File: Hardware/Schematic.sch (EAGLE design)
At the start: 15 parts, among them J1 691311400102, J2 691311400102, K1 ZF112, T1 BC547, U1 HLK-PM01, U2 ESP32-DEVKIT-V1

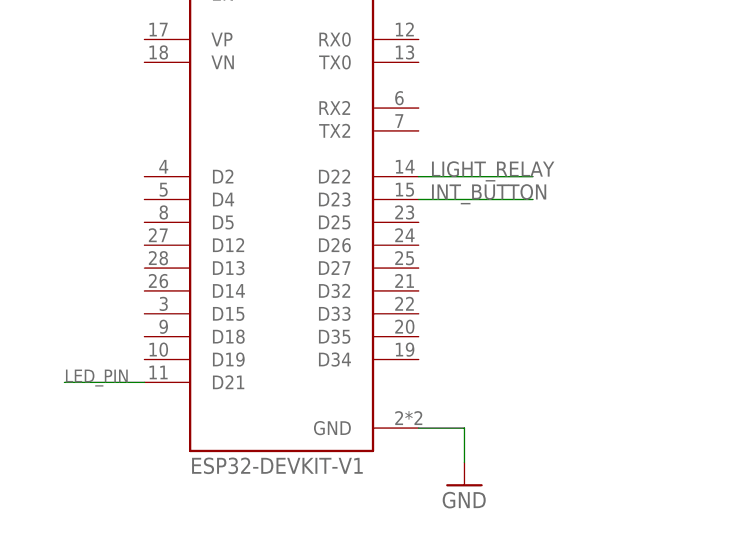
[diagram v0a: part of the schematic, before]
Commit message: Add Interrupt to wake from deep sleep to change the configuration settings
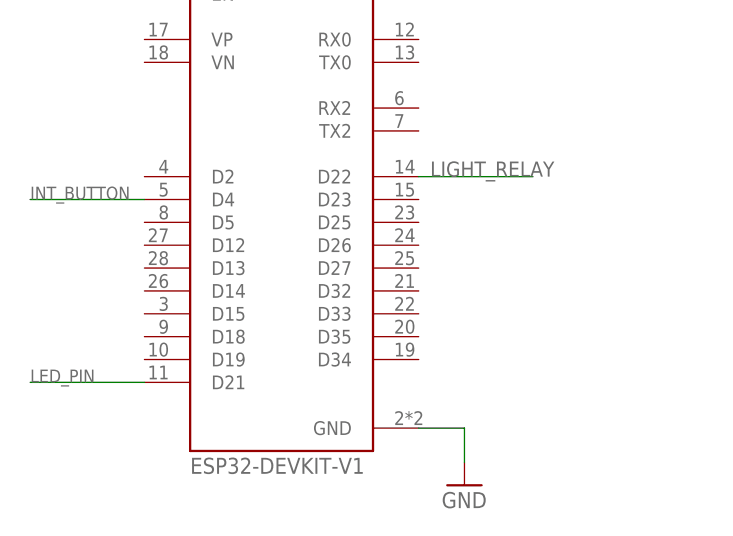
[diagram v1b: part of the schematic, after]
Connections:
- net INT_BUTTON: now also U2.D4; no longer U2.D23
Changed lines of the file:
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@@
 <segment>
 <pinref part="U2" gate="G$1" pin="D21"/>
-<wire x1="17.78" y1="19.05" x2="8.89" y2="19.05" width="0.1524" layer="91"/>
-<label x="8.89" y="19.05" size="1.4224" layer="95" font="vector" ratio="10"/>
+<wire x1="17.78" y1="19.05" x2="5.08" y2="19.05" width="0.1524" layer="91"/>
+<label x="5.08" y="19.05" size="1.4224" layer="95" font="vector" ratio="10"/>
 </segment>
 <segment>
@@
 <net name="INT_BUTTON" class="0">
 <segment>
-<wire x1="60.96" y1="39.37" x2="48.26" y2="39.37" width="0.1524" layer="91"/>
-<pinref part="U2" gate="G$1" pin="D23"/>
-<label x="49.53" y="39.37" size="1.6764" layer="95" font="vector" ratio="10"/>
-</segment>
-<segment>
 <pinref part="SW1" gate="G$1" pin="P$2"/>
 <wire x1="133.35" y1="46.99" x2="137.16" y2="46.99" width="0.1524" layer="91"/>
@@
 <label x="139.7" y="46.99" size="1.6764" layer="95" font="vector" ratio="10"/>
 </segment>
+<segment>
+<pinref part="U2" gate="G$1" pin="D4"/>
+<wire x1="17.78" y1="39.37" x2="5.08" y2="39.37" width="0.1524" layer="91"/>
+<label x="5.08" y="39.37" size="1.4224" layer="95"/>
+</segment>
 </net>
